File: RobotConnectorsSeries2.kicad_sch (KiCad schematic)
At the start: 26 parts, among them J11 Conn_01x03_Male, J12 Conn_01x03_Male, J13 Conn_01x03_Male, Q3 AO3401A, U6 LM339

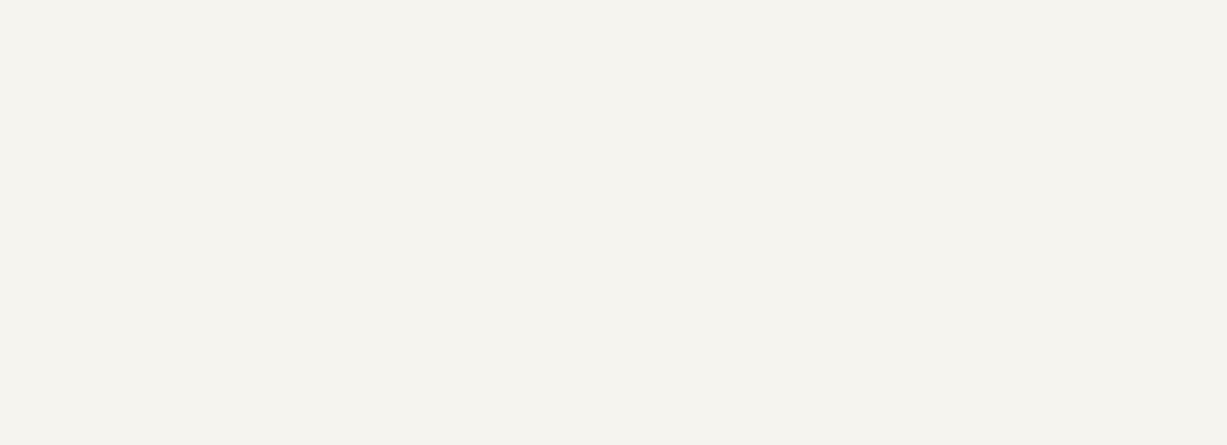
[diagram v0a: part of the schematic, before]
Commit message: Update state and required v0.2 PCB modifications
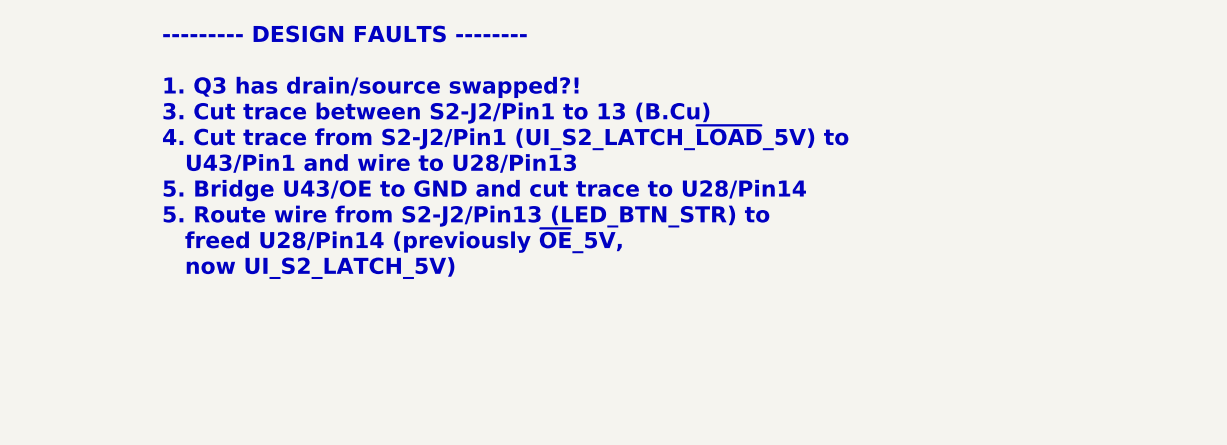
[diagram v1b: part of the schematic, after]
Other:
- note added: "--------- DESIGN FAULTS -------- 1. Q3 has drain/source swapped?! 3. Cut trace between S2-J2/Pin1 to 13 (B.Cu) 4. Cut trace from S2-J2/Pin1 (UI_S2_LATCH_~{LOAD}_5V) to U43/Pin1 and wire to U28/Pin13 5. Bridge U43/OE to GND and cut trace to U28/Pin14 5. Route wire from S2-J2/Pin13 (LED_BTN_STR) to freed U28/Pin14 (previously ~{OE}_5V, now UI_S2_LATCH_5V)"
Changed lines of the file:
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@@
+		)
+	)
+	(text "--------- DESIGN FAULTS --------\n\n1. Q3 has drain/source swapped?!\n3. Cut trace between S2-J2/Pin1 to 13 (B.Cu)\n4. Cut trace from S2-J2/Pin1 (UI_S2_LATCH_~{LOAD}_5V) to\n   U43/Pin1 and wire to U28/Pin13\n5. Bridge U43/OE to GND and cut trace to U28/Pin14\n5. Route wire from S2-J2/Pin13 (LED_BTN_STR) to\n   freed U28/Pin14 (previously ~{OE}_5V,\n   now UI_S2_LATCH_5V)"
+		(exclude_from_sim no)
+		(at 102.616 -12.446 0)
+		(effects
+			(font
+				(size 1.778 1.778)
+				(thickness 0.254)
+				(bold yes)
+				(color 255 0 0 1)
+			)
+			(justify left)
 		)
 	)
@@
 		(stroke
 			(width 0)
-			(type default)
-		)
-	)
+			(type dash_dot)
+			(color 255 18 0 1)
+		)
+	)

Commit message: v0.2 required changes
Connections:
- net LCD_IN_MISC1_3V renamed LCD_~{RST}_3V
- net LCD_IN_MISC2_3V renamed LCD_~{C}D_3V
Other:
- note removed: "--------- DESIGN FAULTS -------- 1. Q3 has drain/source swapped?! 3. Cut trace between S2-J2/Pin1 to 13 (B.Cu) 4. Cut trace from S2-J2/Pin1 (UI_S2_LATCH_~{LOAD}_5V) to U43/Pin1 and wire to U28/Pin13 5. Bridge U43/OE to GND and cut trace to U28/Pin14 5. Route wire from S2-J2/Pin13 (LED_BTN_STR) to freed U28/Pin14 (previously ~{OE}_5V, now UI_S2_LATCH_5V)"
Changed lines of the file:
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@@
-		)
-	)
-	(text "--------- DESIGN FAULTS --------\n\n1. Q3 has drain/source swapped?!\n3. Cut trace between S2-J2/Pin1 to 13 (B.Cu)\n4. Cut trace from S2-J2/Pin1 (UI_S2_LATCH_~{LOAD}_5V) to\n   U43/Pin1 and wire to U28/Pin13\n5. Bridge U43/OE to GND and cut trace to U28/Pin14\n5. Route wire from S2-J2/Pin13 (LED_BTN_STR) to\n   freed U28/Pin14 (previously ~{OE}_5V,\n   now UI_S2_LATCH_5V)"
-		(exclude_from_sim no)
-		(at 102.616 -12.446 0)
-		(effects
-			(font
-				(size 1.778 1.778)
-				(thickness 0.254)
-				(bold yes)
-				(color 255 0 0 1)
-			)
-			(justify left)
 		)
 	)
@@
 		)
 	)
-	(hierarchical_label "LCD_IN_MISC2_3V"
+	(hierarchical_label "LCD_~{C}D_3V"
 		(shape input)
 		(at 180.34 54.61 180)
@@
 		)
 	)
-	(hierarchical_label "LCD_IN_MISC1_3V"
+	(hierarchical_label "LCD_~{RST}_3V"
 		(shape input)
 		(at 209.55 64.77 0)

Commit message: v0.3 prototype
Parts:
- removed J11, J12, J13: Conn_01x03_Male, Connector_JST:JST_XH_B3B-XH-A_1x03_P2.50mm_Vertical, symbol Connector:Conn_01x03_Male
- removed Q3: AO3401A, Package_TO_SOT_SMD:SOT-23, symbol Transistor_FET:AO3401A
- removed R39, R40: 10k, Resistor_SMD:R_0603_1608Metric_Pad0.98x0.95mm_HandSolder, symbol Device:R
- removed R91: 10k, Resistor_SMD:R_0402_1005Metric, symbol Device:R
- removed S2-J8: Conn_02x05_Odd_Even, local_Connectors:Molex_Milli-Grid_878311041, symbol Connector_Generic:Conn_02x05_Odd_Even
- removed U6: LM339, Package_SO:SOIC-14_3.9x8.7mm_P1.27mm, symbol Comparator:LM339
- added C95: 100nF, Capacitor_SMD:C_0402_1005Metric, symbol Device:C
- added JP2: SolderJumper_2_Bridged, Jumper:SolderJumper-2_P1.3mm_Bridged_RoundedPad1.0x1.5mm, symbol Jumper:SolderJumper_2_Bridged
- added U49, U50: LM2903DR, Package_SO:SOIC-8_3.9x4.9mm_P1.27mm, symbol Comparator:LM2903
- R89, R90: now not fitted; now left out of the parts list
- S2-J5, S2-J6: FT Rotation Offset 0 -> 90; LCSC Part # C400369 -> C505075
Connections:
- net 5V_HALL is gone; now on net 5V: C53.1, C87.1, R41.1, R42.1, R89.1, S2-J7.3 (Pin_3)
- net BTN_~{CE}_5V is gone; now on net GND: S2-J2.8 (Pin_8)
- net 1.24V_REF_A: now also U50.5 (+)
- net 5V: now also C95.1, U49.8 (V+), U50.8 (V+)
- net GND: now also C95.2, U49.4 (V-), U50.2 (-), U50.3 (+), U50.4 (V-)
- net HALL0_5V: now also U49.7
- net HALL1_5V: now also U49.1
- net HALL2_5V: now also U50.7
- net at R10.1, S2-J7.1 (Pin_1): now also U49.6 (-)
- net at R27.1, S2-J7.2 (Pin_2): now also U49.2 (-)
- net at R28.1, S2-J2.6 (Pin_6): now also U50.6 (-)
- net 1.24V_REF_B: no longer names the net of R89.2, R90.1
- net 1.24V_REF_B: now also JP2.1 (A), U49.5 (+)
- net 1.24V_REF_D: no longer names the net of R23.1, R41.2
- net 1.24V_REF_D: now also JP2.2 (B), U49.3 (+)
- net BMC_GN renamed BMC_SPI_MISO
- net BMC_YW renamed BMC_SPI_CLK
- net LATCH_LOAD_5V renamed BTN_SH/~{LD}_5V
- net BTN_SH/~{LD}_5V: no longer S2-J2.13 (Pin_13)
- net OE_5V renamed LED_BTN_OE_5V
- net SPI_RX_5V renamed SPI_MISO_5V
- net SPI_TX_5V renamed SPI_MOSI_5V
- new net LED_BTN_STR_5V: S2-J2.13 (Pin_13)
- no-connect marks 22 -> 12
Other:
- note added: "1.24V_REF_A"
- note added: "1.24V_REF_B"
- note added: "BTN_~{CE}_5V"
- note removed: "Backup plan"
- moved on the sheet: C53, C87, R10, R23, R27, R41, S2-J10, S2-J7

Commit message: BOM optimization
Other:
- title: OpenMower SABO Mainboard for Series I & II -> OpenMower SABO Carrierboard for Series I & II
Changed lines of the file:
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@@
 	(paper "A4")
 	(title_block
-		(title "OpenMower SABO Mainboard for Series I & II")
-		(date "2025-10-05")
-		(rev "v0.3")
+		(title "OpenMower SABO Carrierboard for Series I & II")
+		(date "2025-10-12")
+		(rev "v0.4")
 		(company "Apeheanger <joerg@ebeling.ws> for OpenMower")
 		(comment 1 "This design is licensed under CC BY-NC 4.0")

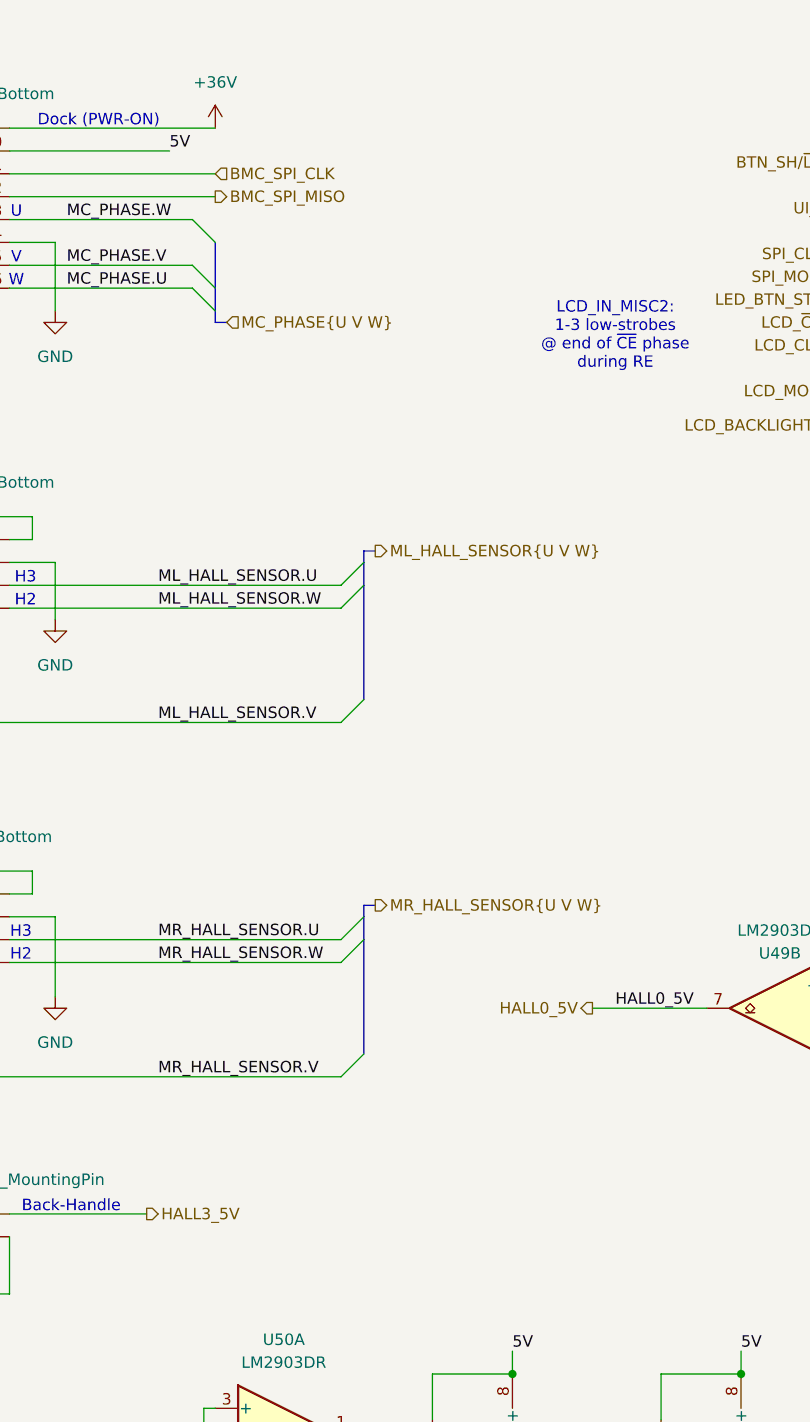
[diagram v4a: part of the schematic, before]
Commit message: Typo BMC to BMS
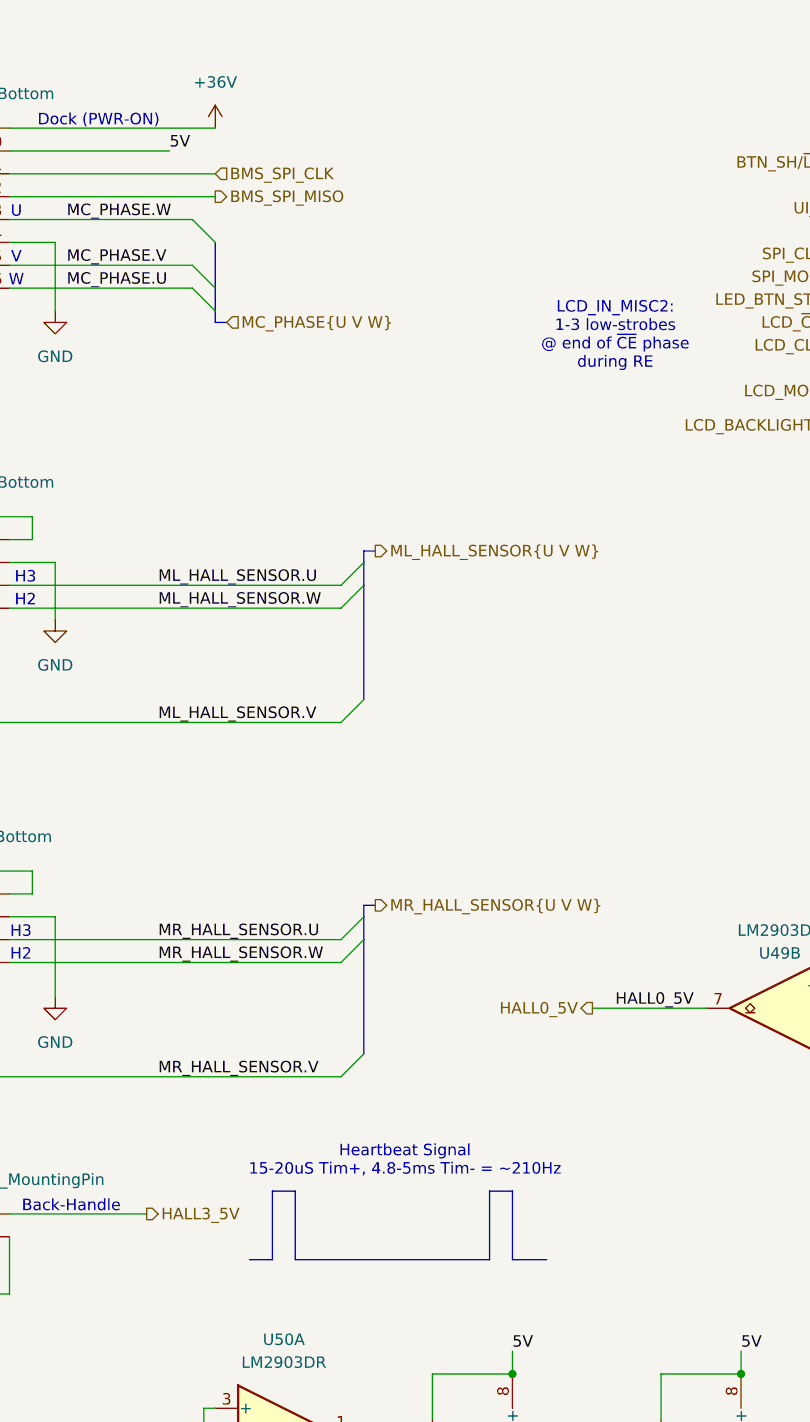
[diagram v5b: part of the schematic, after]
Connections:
- net BMC_SPI_CLK renamed BMS_SPI_CLK
- net BMC_SPI_MISO renamed BMS_SPI_MISO
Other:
- note added: "Heartbeat Signal 15-20uS Tim+, 4.8-5ms Tim- = ~210Hz"
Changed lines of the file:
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@@
+		)
+	)
+	(text "Heartbeat Signal\n15-20uS Tim+, 4.8-5ms Tim- = ~210Hz"
+		(exclude_from_sim no)
+		(at 129.032 147.828 0)
+		(effects
+			(font
+				(size 1.27 1.27)
+			)
 		)
 	)
@@
 		)
 	)
+	(polyline
+		(pts
+			(xy 138.43 151.13) (xy 140.97 151.13)
+		)
+		(stroke
+			(width 0)
+			(type default)
+		)
+	)
 	(wire
 		(pts
@@
 		)
 	)
+	(polyline
+		(pts
+			(xy 114.3 151.13) (xy 116.84 151.13)
+		)
+		(stroke
+			(width 0)
+			(type default)
+		)
+	)
 	(bus
 		(pts
@@
 		)
 	)
+	(polyline
+		(pts
+			(xy 116.84 151.13) (xy 116.84 158.75)
+		)
+		(stroke
+			(width 0)
+			(type default)
+		)
+	)
 	(wire
 		(pts
@@
 		)
 	)
+	(polyline
+		(pts
+			(xy 111.76 158.75) (xy 114.3 158.75)
+		)
+		(stroke
+			(width 0)
+			(type default)
+		)
+	)
 	(wire
 		(pts
@@
 		)
 	)
+	(polyline
+		(pts
+			(xy 138.43 158.75) (xy 138.43 151.13)
+		)
+		(stroke
+			(width 0)
+			(type default)
+		)
+	)
 	(wire
 		(pts
@@
 		)
 	)
+	(polyline
+		(pts
+			(xy 140.97 158.75) (xy 144.78 158.75)
+		)
+		(stroke
+			(width 0)
+			(type default)
+		)
+	)
 	(wire
 		(pts
@@
 		)
 	)
+	(polyline
+		(pts
+			(xy 114.3 158.75) (xy 114.3 151.13)
+		)
+		(stroke
+			(width 0)
+			(type default)
+		)
+	)
 	(wire
 		(pts
@@
 		)
 	)
+	(polyline
+		(pts
+			(xy 140.97 151.13) (xy 140.97 158.75)
+		)
+		(stroke
+			(width 0)
+			(type default)
+		)
+	)
 	(wire
 		(pts
@@
 		(pts
 			(xy 124.46 80.01) (xy 124.46 81.28)
+		)
+		(stroke
+			(width 0)
+			(type default)
+		)
+	)
+	(polyline
+		(pts
+			(xy 116.84 158.75) (xy 138.43 158.75)
 		)
 		(stroke
@@
 		)
 	)
-	(hierarchical_label "BMC_SPI_CLK"
+	(hierarchical_label "BMS_SPI_CLK"
 		(shape input)
 		(at 107.95 38.1 0)
@@
 		)
 	)
-	(hierarchical_label "BMC_SPI_MISO"
+	(hierarchical_label "BMS_SPI_MISO"
 		(shape output)
 		(at 107.95 40.64 0)

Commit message: Add latest findings
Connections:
- net BMS_SPI_CLK renamed BMS_I2C_SCL
- net BMS_SPI_MISO renamed BMS_I2C_SDA
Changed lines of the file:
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@@
 		)
 	)
-	(hierarchical_label "BMS_SPI_CLK"
+	(hierarchical_label "BMS_I2C_SCL"
 		(shape input)
 		(at 107.95 38.1 0)
@@
 		)
 	)
-	(hierarchical_label "BMS_SPI_MISO"
+	(hierarchical_label "BMS_I2C_SDA"
 		(shape output)
 		(at 107.95 40.64 0)

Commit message: Prepare for next production - Slightly adapt part selection - Add TC2050 holes
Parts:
- C53, C87, C95: JLC C307331 -> (none); LCSC Part # (none) -> C307331
- R10, R27, R28: JLC C22787 -> (none); LCSC Part # (none) -> C22787
- R23, R43: JLC C22978 -> (none); LCSC Part # (none) -> C22978
- R41, R42: JLC C25804 -> (none); LCSC Part # (none) -> C25804
- R89: JLC C25804 -> (none)
- R90: JLC C22978 -> (none)
- S2-J1: JLC C5339222 -> (none); LCSC Part # (none) -> C5339222
- S2-J10: JLC C293535 -> (none); LCSC Part # (none) -> C293535
- S2-J2: JLC C17215745 -> (none); LCSC Part # (none) -> C916288
- S2-J5, S2-J6: MF (none) -> Molex; Manufacturer Molex -> (none)

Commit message: Next proto prep
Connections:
- net LED_BTN_OE_5V is gone; now on net 5V: S2-J2.14 (Pin_14)
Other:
- note added: "LED_BTN_OE_5V"
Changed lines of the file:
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@@
+		)
+	)
+	(text "LED_BTN_OE_5V"
+		(exclude_from_sim no)
+		(at 215.138 52.07 0)
+		(effects
+			(font
+				(size 1.27 1.27)
+			)
 		)
 	)
@@
 	)
 	(junction
+		(at 207.01 49.53)
+		(diameter 0)
+		(color 0 0 0 0)
+	)
+	(junction
 		(at 140.97 186.69)
 		(diameter 0)
@@
 	(wire
 		(pts
-			(xy 204.47 52.07) (xy 209.55 52.07)
+			(xy 204.47 52.07) (xy 207.01 52.07)
 		)
 		(stroke
@@
 		(pts
 			(xy 68.58 45.72) (xy 68.58 33.02)
+		)
+		(stroke
+			(width 0)
+			(type default)
+		)
+	)
+	(wire
+		(pts
+			(xy 207.01 49.53) (xy 207.01 52.07)
 		)
 		(stroke
@@
 		(effects
 			(font
-				(size 1.27 1.27)
-			)
-			(justify left)
-		)
-	)
-	(hierarchical_label "LED_BTN_OE_5V"
-		(shape input)
-		(at 209.55 52.07 0)
-		(effects
-			(font
